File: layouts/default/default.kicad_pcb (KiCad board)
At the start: 2 copper layers, 7 parts

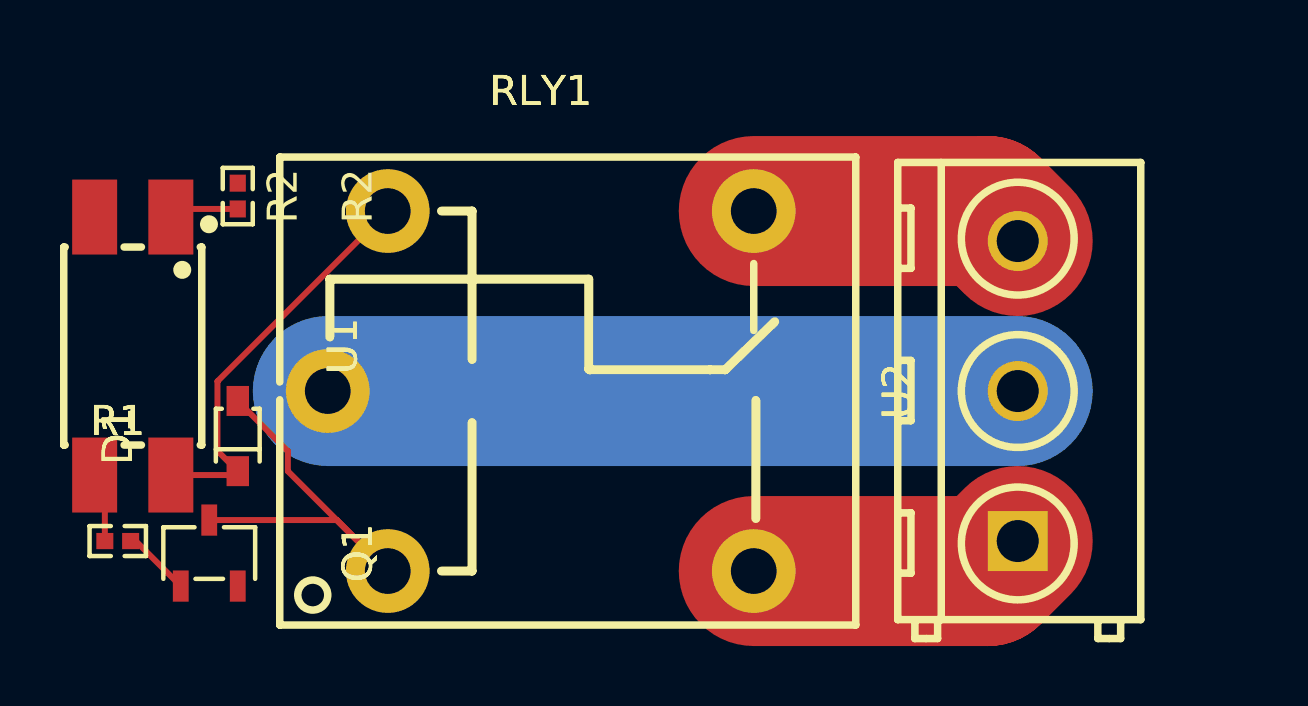
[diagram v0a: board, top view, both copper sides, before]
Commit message: Swapped out the connecter with a pluggable one.
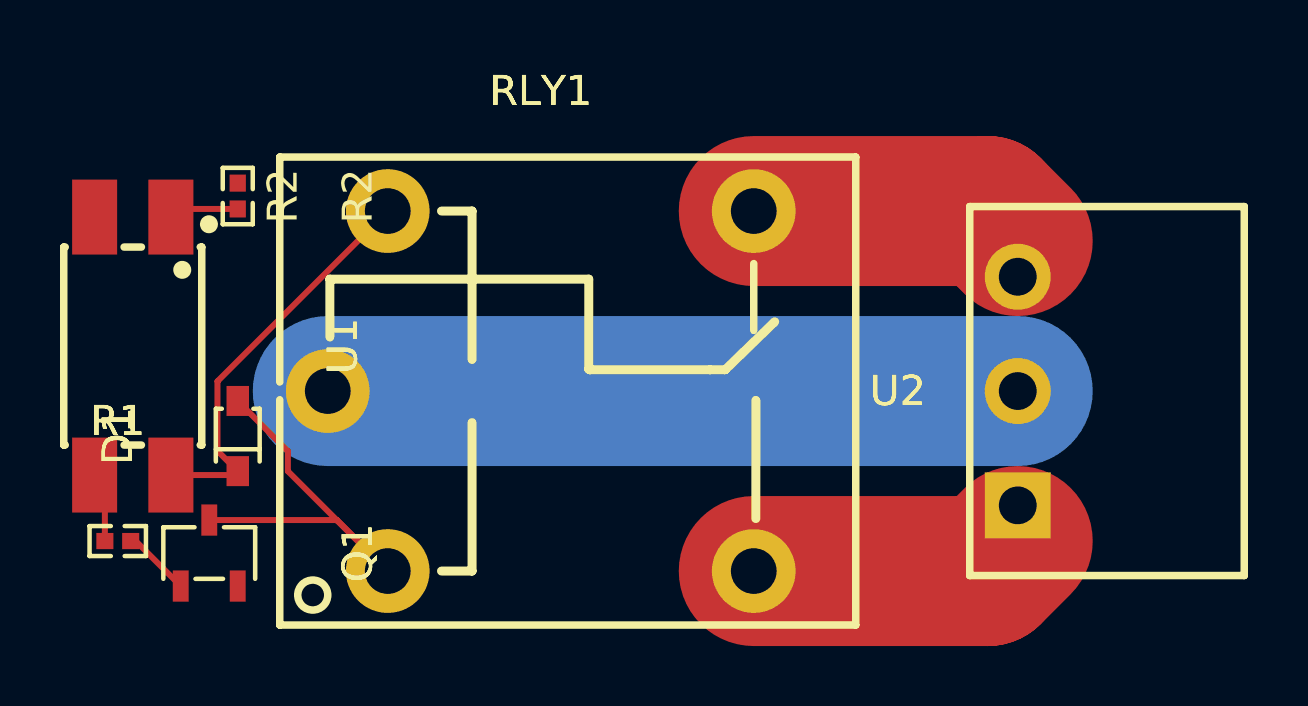
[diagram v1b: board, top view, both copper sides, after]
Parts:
- U2: footprint DIBO_DB127V_5_08_3P_GN_S:CONN-TH_3P-P5.08_DB127V-5.08-3P-GN-S -> Ningbo_Kangnex_Elec_WJ15EDGRC_3_81_3P:CONN-TH_3P-P3.81_WJ15EDGRC-3.81-3P
